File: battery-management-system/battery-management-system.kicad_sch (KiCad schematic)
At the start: 0 parts

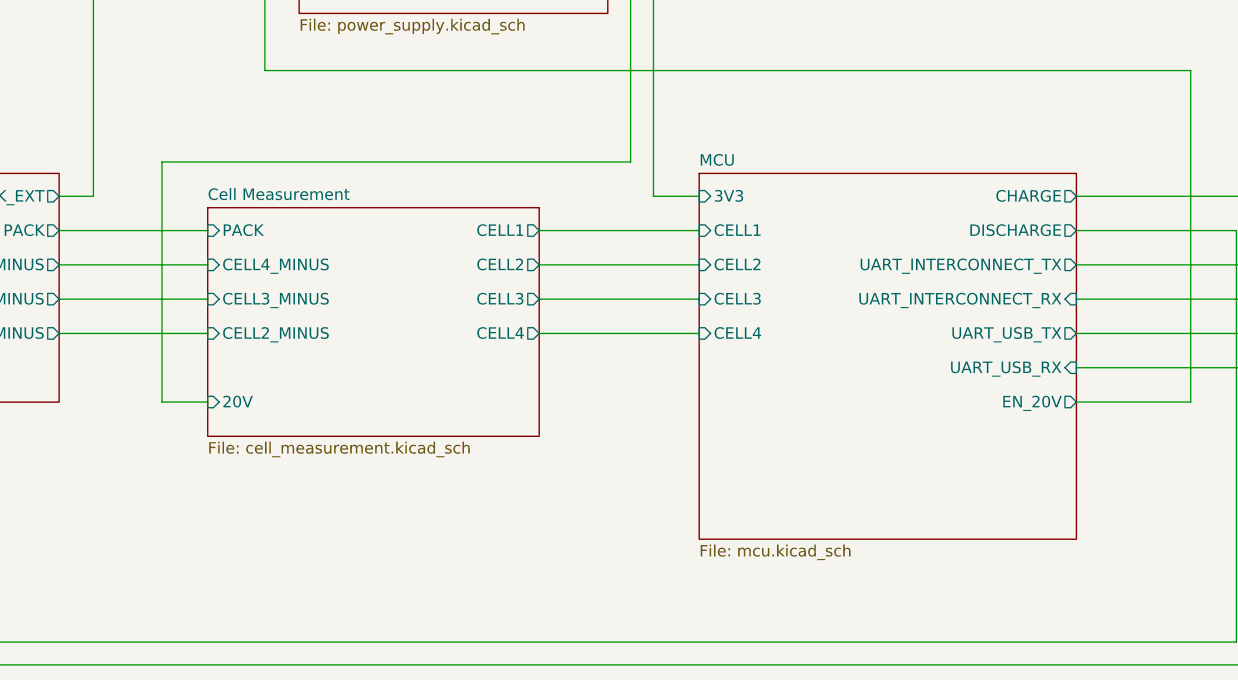
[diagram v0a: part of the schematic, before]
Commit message: improve usage of net labels
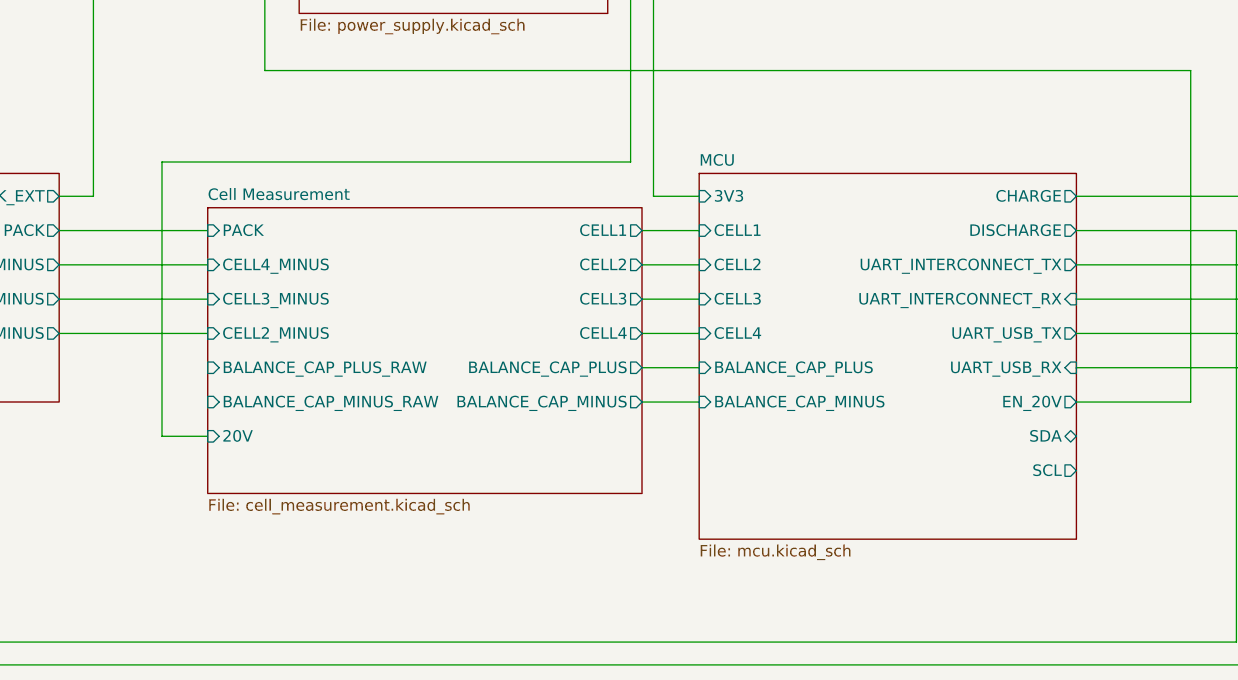
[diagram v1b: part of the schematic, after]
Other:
- sheet Cell Measurement ports: added BALANCE_CAP_MINUS, BALANCE_CAP_MINUS_RAW, BALANCE_CAP_PLUS, BALANCE_CAP_PLUS_RAW; removed none
- sheet MCU ports: added BALANCE_CAP_MINUS, BALANCE_CAP_PLUS, SCL, SDA; removed none
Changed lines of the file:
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@@
     (stroke (width 0) (type default))
   )
-  (wire (pts (xy 78.74 100.33) (xy 83.82 100.33))
+  (wire (pts (xy 78.74 104.14) (xy 83.82 104.14))
     (stroke (width 0) (type default))
   )
@@
     (stroke (width 0) (type default))
   )
-  (wire (pts (xy 120.65 85.09) (xy 138.43 85.09))
-    (stroke (width 0) (type default))
-  )
   (wire (pts (xy 67.31 85.09) (xy 83.82 85.09))
     (stroke (width 0) (type default))
@@
     (stroke (width 0) (type default))
   )
-  (wire (pts (xy 120.65 88.9) (xy 138.43 88.9))
+  (wire (pts (xy 132.08 96.52) (xy 138.43 96.52))
     (stroke (width 0) (type default))
   )
@@
     (stroke (width 0) (type default))
   )
-  (wire (pts (xy 120.65 81.28) (xy 138.43 81.28))
+  (wire (pts (xy 132.08 85.09) (xy 138.43 85.09))
+    (stroke (width 0) (type default))
+  )
+  (wire (pts (xy 132.08 81.28) (xy 138.43 81.28))
     (stroke (width 0) (type default))
   )
@@
     (stroke (width 0) (type default))
   )
-  (wire (pts (xy 120.65 92.71) (xy 138.43 92.71))
-    (stroke (width 0) (type default))
-  )
   (wire (pts (xy 90.17 36.83) (xy 90.17 46.99))
     (stroke (width 0) (type default))
@@
     (stroke (width 0) (type default))
   )
+  (wire (pts (xy 132.08 92.71) (xy 138.43 92.71))
+    (stroke (width 0) (type default))
+  )
   (wire (pts (xy 207.01 46.99) (xy 207.01 81.28))
     (stroke (width 0) (type default))
@@
     (stroke (width 0) (type default))
   )
+  (wire (pts (xy 132.08 100.33) (xy 138.43 100.33))
+    (stroke (width 0) (type default))
+  )
   (wire (pts (xy 128.27 50.8) (xy 130.81 50.8))
     (stroke (width 0) (type default))
@@
     (stroke (width 0) (type default))
   )
-  (wire (pts (xy 78.74 73.66) (xy 78.74 100.33))
+  (wire (pts (xy 78.74 73.66) (xy 78.74 104.14))
     (stroke (width 0) (type default))
   )
@@
   )
   (wire (pts (xy 71.12 43.18) (xy 93.98 43.18))
+    (stroke (width 0) (type default))
+  )
+  (wire (pts (xy 132.08 88.9) (xy 138.43 88.9))
     (stroke (width 0) (type default))
   )
@@
     )
   )
-  (sheet (at 83.82 78.74) (size 36.83 25.4) (fields_autoplaced)
+  (sheet (at 83.82 78.74) (size 48.26 31.75) (fields_autoplaced)
     (stroke (width 0.1524) (type solid))
     (fill (color 0 0 0 0.0000))
@@
       (effects (font (size 1.27 1.27)) (justify left bottom))
     )
-    (property "Sheetfile" "cell_measurement.kicad_sch" (at 83.82 104.7246 0)
+    (property "Sheetfile" "cell_measurement.kicad_sch" (at 83.82 111.0746 0)
       (effects (font (size 1.27 1.27)) (justify left top))
     )
@@
       (effects (font (size 1.27 1.27)) (justify left))
     )
-    (pin "20V" input (at 83.82 100.33 180)
-      (effects (font (size 1.27 1.27)) (justify left))
-    )
-    (pin "CELL1" output (at 120.65 81.28 0)
-      (effects (font (size 1.27 1.27)) (justify right))
-    )
-    (pin "CELL2" output (at 120.65 85.09 0)
-      (effects (font (size 1.27 1.27)) (justify right))
-    )
-    (pin "CELL3" output (at 120.65 88.9 0)
-      (effects (font (size 1.27 1.27)) (justify right))
-    )
-    (pin "CELL4" output (at 120.65 92.71 0)
+    (pin "20V" input (at 83.82 104.14 180)
+      (effects (font (size 1.27 1.27)) (justify left))
+    )
+    (pin "CELL1" output (at 132.08 81.28 0)
+      (effects (font (size 1.27 1.27)) (justify right))
+    )
+    (pin "CELL2" output (at 132.08 85.09 0)
+      (effects (font (size 1.27 1.27)) (justify right))
+    )
+    (pin "CELL3" output (at 132.08 88.9 0)
+      (effects (font (size 1.27 1.27)) (justify right))
+    )
+    (pin "CELL4" output (at 132.08 92.71 0)
+      (effects (font (size 1.27 1.27)) (justify right))
+    )
+    (pin "BALANCE_CAP_PLUS_RAW" input (at 83.82 96.52 180)
+      (effects (font (size 1.27 1.27)) (justify left))
+    )
+    (pin "BALANCE_CAP_MINUS_RAW" input (at 83.82 100.33 180)
+      (effects (font (size 1.27 1.27)) (justify left))
+    )
+    (pin "BALANCE_CAP_PLUS" output (at 132.08 96.52 0)
+      (effects (font (size 1.27 1.27)) (justify right))
+    )
+    (pin "BALANCE_CAP_MINUS" output (at 132.08 100.33 0)
       (effects (font (size 1.27 1.27)) (justify right))
     )
@@
       (effects (font (size 1.27 1.27)) (justify right))
     )
+    (pin "BALANCE_CAP_PLUS" input (at 138.43 96.52 180)
+      (effects (font (size 1.27 1.27)) (justify left))
+    )
+    (pin "BALANCE_CAP_MINUS" input (at 138.43 100.33 180)
+      (effects (font (size 1.27 1.27)) (justify left))
+    )
+    (pin "SDA" bidirectional (at 180.34 104.14 0)
+      (effects (font (size 1.27 1.27)) (justify right))
+    )
+    (pin "SCL" output (at 180.34 107.95 0)
+      (effects (font (size 1.27 1.27)) (justify right))
+    )

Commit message: update PCB
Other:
- added sheet Temperature Sensors (temperature_sensors.kicad_sch)
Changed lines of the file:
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@@
 (kicad_sch (version 20230121) (generator eeschema)
   (paper "A4")
+  (junction (at 208.28 104.14) (diameter 0) (color 0 0 0 0)
+  )
   (junction (at 133.35 43.18) (diameter 0) (color 0 0 0 0)
   )
@@
     (stroke (width 0) (type default))
   )
-  (wire (pts (xy 24.13 129.54) (xy 200.66 129.54))
-    (stroke (width 0) (type default))
-  )
-  (wire (pts (xy 198.12 81.28) (xy 198.12 127))
-    (stroke (width 0) (type default))
-  )
-  (wire (pts (xy 200.66 129.54) (xy 200.66 77.47))
+  (wire (pts (xy 22.86 152.4) (xy 199.39 152.4))
+    (stroke (width 0) (type default))
+  )
+  (wire (pts (xy 180.34 104.14) (xy 194.31 104.14))
+    (stroke (width 0) (type default))
+  )
+  (wire (pts (xy 196.85 81.28) (xy 196.85 149.86))
+    (stroke (width 0) (type default))
+  )
+  (wire (pts (xy 199.39 152.4) (xy 199.39 77.47))
     (stroke (width 0) (type default))
   )
@@
     (stroke (width 0) (type default))
   )
+  (wire (pts (xy 208.28 104.14) (xy 208.28 125.73))
+    (stroke (width 0) (type default))
+  )
   (wire (pts (xy 67.31 85.09) (xy 83.82 85.09))
     (stroke (width 0) (type default))
@@
     (stroke (width 0) (type default))
   )
+  (wire (pts (xy 191.77 133.35) (xy 210.82 133.35))
+    (stroke (width 0) (type default))
+  )
+  (wire (pts (xy 194.31 129.54) (xy 210.82 129.54))
+    (stroke (width 0) (type default))
+  )
   (wire (pts (xy 132.08 96.52) (xy 138.43 96.52))
     (stroke (width 0) (type default))
@@
     (stroke (width 0) (type default))
   )
+  (wire (pts (xy 194.31 104.14) (xy 194.31 129.54))
+    (stroke (width 0) (type default))
+  )
   (wire (pts (xy 180.34 92.71) (xy 205.74 92.71))
     (stroke (width 0) (type default))
   )
+  (wire (pts (xy 208.28 125.73) (xy 210.82 125.73))
+    (stroke (width 0) (type default))
+  )
   (wire (pts (xy 205.74 92.71) (xy 205.74 107.95))
     (stroke (width 0) (type default))
@@
     (stroke (width 0) (type default))
   )
-  (wire (pts (xy 26.67 127) (xy 198.12 127))
+  (wire (pts (xy 25.4 149.86) (xy 196.85 149.86))
     (stroke (width 0) (type default))
   )
@@
     (stroke (width 0) (type default))
   )
+  (wire (pts (xy 191.77 107.95) (xy 191.77 133.35))
+    (stroke (width 0) (type default))
+  )
   (wire (pts (xy 180.34 88.9) (xy 210.82 88.9))
     (stroke (width 0) (type default))
@@
     (stroke (width 0) (type default))
   )
-  (wire (pts (xy 180.34 81.28) (xy 198.12 81.28))
-    (stroke (width 0) (type default))
-  )
-  (wire (pts (xy 24.13 129.54) (xy 24.13 77.47))
-    (stroke (width 0) (type default))
-  )
-  (wire (pts (xy 26.67 127) (xy 26.67 81.28))
+  (wire (pts (xy 180.34 81.28) (xy 196.85 81.28))
+    (stroke (width 0) (type default))
+  )
+  (wire (pts (xy 22.86 152.4) (xy 22.86 77.47))
+    (stroke (width 0) (type default))
+  )
+  (wire (pts (xy 180.34 107.95) (xy 191.77 107.95))
+    (stroke (width 0) (type default))
+  )
+  (wire (pts (xy 25.4 149.86) (xy 25.4 81.28))
     (stroke (width 0) (type default))
   )
@@
     (stroke (width 0) (type default))
   )
-  (wire (pts (xy 26.67 81.28) (xy 31.75 81.28))
+  (wire (pts (xy 25.4 81.28) (xy 31.75 81.28))
     (stroke (width 0) (type default))
   )
@@
     (stroke (width 0) (type default))
   )
-  (wire (pts (xy 24.13 77.47) (xy 31.75 77.47))
+  (wire (pts (xy 22.86 77.47) (xy 31.75 77.47))
     (stroke (width 0) (type default))
   )
@@
     (stroke (width 0) (type default))
   )
-  (wire (pts (xy 180.34 77.47) (xy 200.66 77.47))
+  (wire (pts (xy 180.34 77.47) (xy 199.39 77.47))
     (stroke (width 0) (type default))
   )
@@
     )
   )
+  (sheet (at 210.82 123.19) (size 30.48 17.78) (fields_autoplaced)
+    (stroke (width 0.1524) (type solid))
+    (fill (color 0 0 0 0.0000))
+    (property "Sheetname" "Temperature Sensors" (at 210.82 122.4784 0)
+      (effects (font (size 1.27 1.27)) (justify left bottom))
+    )
+    (property "Sheetfile" "temperature_sensors.kicad_sch" (at 210.82 141.5546 0)
+      (effects (font (size 1.27 1.27)) (justify left top))
+    )
+    (pin "SCL" input (at 210.82 129.54 180)
+      (effects (font (size 1.27 1.27)) (justify left))
+    )
+    (pin "3V3" input (at 210.82 125.73 180)
+      (effects (font (size 1.27 1.27)) (justify left))
+    )
+    (pin "SDA" bidirectional (at 210.82 133.35 180)
+      (effects (font (size 1.27 1.27)) (justify left))
+    )
+    (instances
+      (project "battery-management-system"
+        (path "/5272f0ff-3069-41a9-bca2-80beede8b4b2" (page "8"))
+      )
+    )
+  )
   (sheet (at 83.82 78.74) (size 48.26 31.75) (fields_autoplaced)
     (stroke (width 0.1524) (type solid))
@@
       (effects (font (size 1.27 1.27)) (justify left))
     )
-    (pin "SDA" bidirectional (at 180.34 104.14 0)
-      (effects (font (size 1.27 1.27)) (justify right))
-    )
-    (pin "SCL" output (at 180.34 107.95 0)
-      (effects (font (size 1.27 1.27)) (justify right))
-    )
+    (pin "SDA" bidirectional (at 180.34 107.95 0)
+      (effects (font (size 1.27 1.27)) (justify right))
+    )
+    (pin "SCL" output (at 180.34 104.14 0)
+      (effects (font (size 1.27 1.27)) (justify right))
+    )

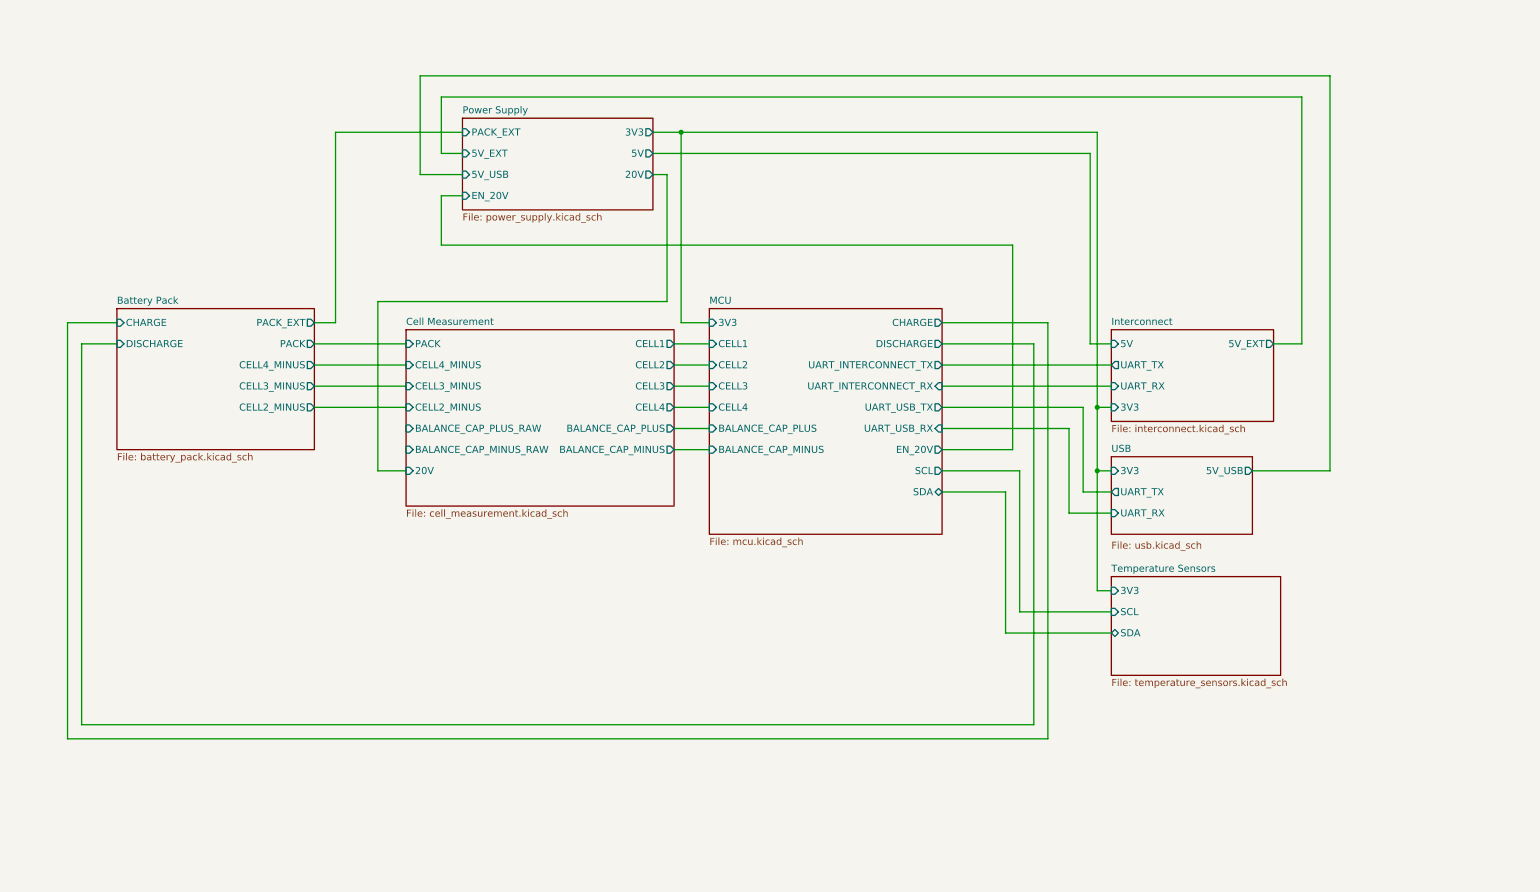
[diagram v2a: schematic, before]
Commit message: add balancing sheet
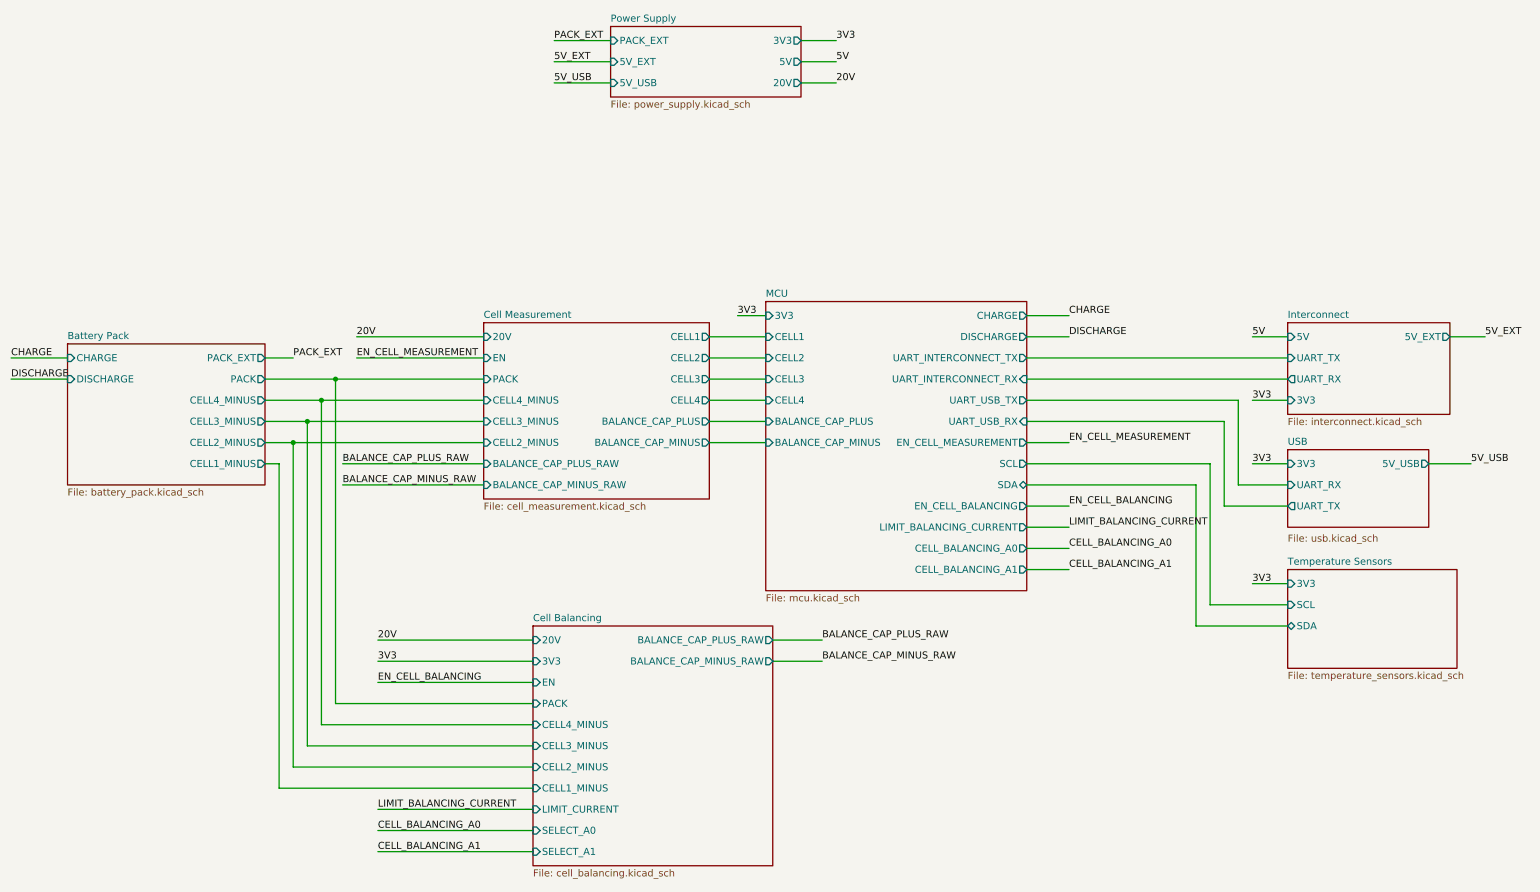
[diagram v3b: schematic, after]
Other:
- added sheet Cell Balancing (cell_balancing.kicad_sch)
- sheet Battery Pack ports: added CELL1_MINUS; removed none
- sheet Cell Measurement ports: added EN; removed none
- sheet MCU ports: added CELL_BALANCING_A0, CELL_BALANCING_A1, EN_CELL_BALANCING, EN_CELL_MEASUREMENT, LIMIT_BALANCING_CURRENT; removed EN_20V
- sheet Power Supply ports: added none; removed EN_20V
